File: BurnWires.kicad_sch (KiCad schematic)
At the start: 24 parts, among them K1 IM11DGR, Q15 IRFTS9342PBF, Q17 IRFTS9342PBF, Q19 IRFTS9342PBF

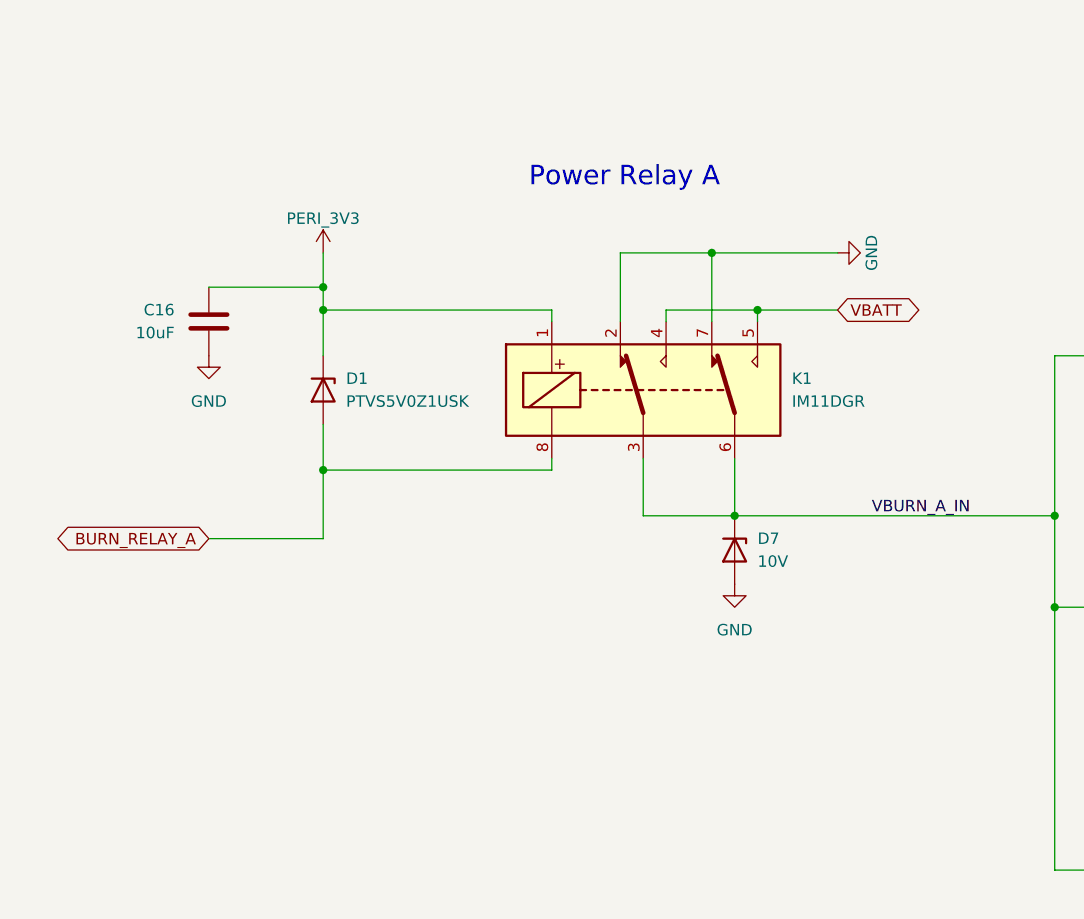
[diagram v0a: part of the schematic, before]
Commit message: Added more silkscreen, switched to PMOS instead of mech relay
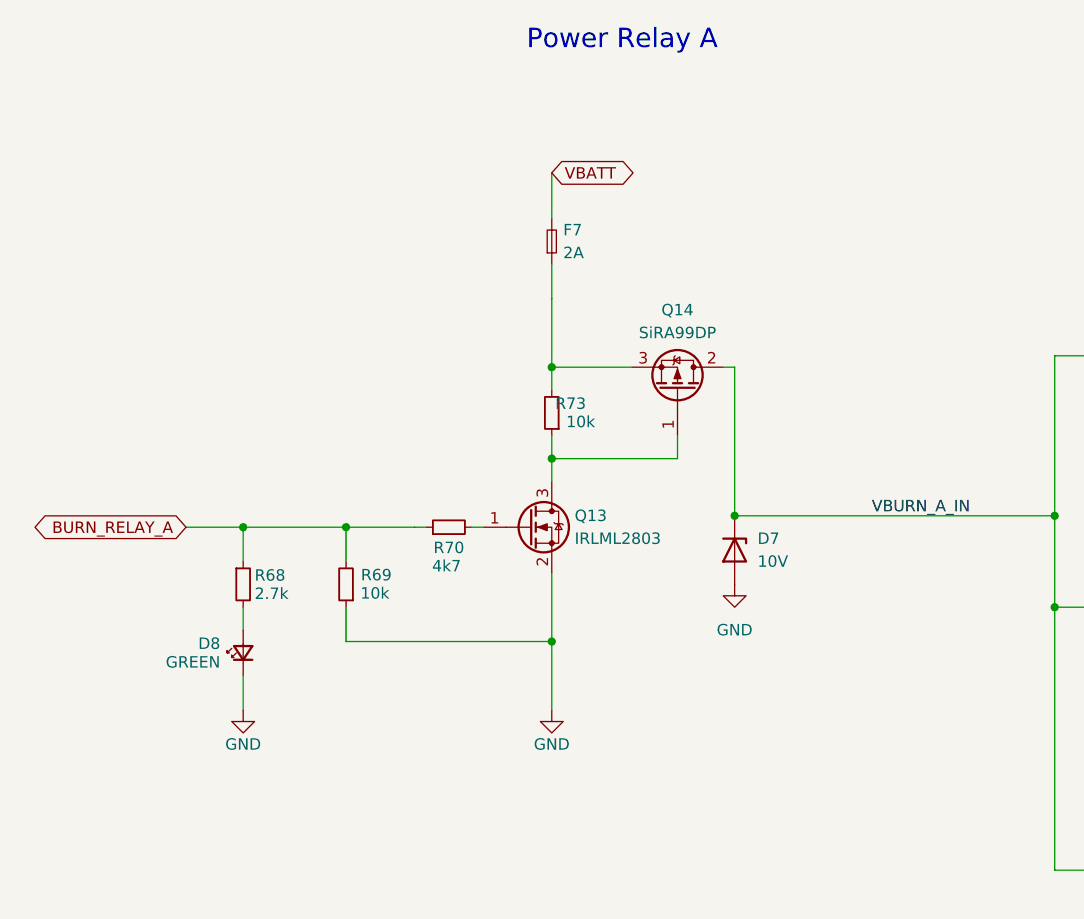
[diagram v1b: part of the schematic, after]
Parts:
- removed C16: 10uF, Capacitor_SMD:C_1206_3216Metric, symbol Device:C
- removed D1: PTVS5V0Z1USK, Diode_SMD:Nexperia_DSN1608-2_1.6x0.8mm, symbol Diode:PTVS5V0Z1USK
- removed K1: IM11DGR, Argus-Miscellaneous:RELAY8_SMTGUL_TEC, symbol Relay:IM02
- added D8: GREEN, LED_SMD:LED_0603_1608Metric, symbol Device:LED_Small
- added F7: 2A, Fuse:Fuse_0603_1608Metric, symbol Device:Fuse_Small
- added Q13: IRLML2803, Package_TO_SOT_SMD:SOT-23, symbol Argus-IC:IRLML2803
- added Q14: SiRA99DP, Argus-Miscellaneous:PowerPAK SO-8, symbol Argus-IC:Q_PMOS_GDS
- added R68: 2.7k, Resistor_SMD:R_0603_1608Metric, symbol Device:R_Small
- added R69, R73: 10k, Resistor_SMD:R_0603_1608Metric, symbol Device:R_Small
- added R70: 4k7, Resistor_SMD:R_0603_1608Metric, symbol Device:R_Small
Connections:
- net BURN_RELAY_A: now also R68.1, R69.2, R70.1
- net GND: now also D8.1 (K), Q13.2 (S), R69.1
- net VBATT: now also F7.2
- net VBURN_A_IN: now also Q14.2 (D)
- new net: Q13.3 (D), Q14.1 (G), R73.1
- new net: F7.1, Q14.3 (S), R73.2
- new net: D8.2 (A), R68.2
- new net: Q13.1 (G), R70.2
